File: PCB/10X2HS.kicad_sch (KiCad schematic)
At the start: 23 parts, among them SW1 SW, SW10 SW, SW11 SW, SW12 SW, SW13 SW, SW14 SW, SW15 SW, SW16 SW, SW17 SW, SW18 SW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

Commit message: more updates I guess
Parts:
- removed SW22: SW_Push, Button_Switch_SMD:Panasonic_EVQPUL_EVQPUC, symbol Switch:SW_Push
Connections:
- net SOFT_OFF: no longer names the net of U2.12 (3V3)
- no-connect marks 0 -> 1
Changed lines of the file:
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@@
 		(color 0 0 0 0)
+	)
+	(no_connect
+		(at 64.77 73.66)
 	)
 	(wire
@@
 		)
 	)
-	(global_label "SOFT_OFF"
-		(shape input)
-		(at 88.9 100.33 180)
-		(effects
-			(font
-				(size 1.27 1.27)
-			)
-			(justify right)
-		)
-		(property "Intersheetrefs" "${INTERSHEET_REFS}"
-			(at 88.9 100.33 0)
-			(effects
-				(font
-					(size 1.27 1.27)
-				)
-				(hide yes)
-			)
-		)
-	)
 	(global_label "SW17"
 		(shape input)
@@
 		)
 	)
-	(global_label "GND"
-		(shape input)
-		(at 99.06 100.33 0)
-		(effects
-			(font
-				(size 1.27 1.27)
-			)
-			(justify left)
-		)
-		(property "Intersheetrefs" "${INTERSHEET_REFS}"
-			(at 99.06 100.33 0)
-			(effects
-				(font
-					(size 1.27 1.27)
-				)
-				(hide yes)
-			)
-		)
-	)
 	(global_label "VCC"
 		(shape input)
@@
 		(property "Intersheetrefs" "${INTERSHEET_REFS}"
 			(at 64.77 91.44 0)
-			(effects
-				(font
-					(size 1.27 1.27)
-				)
-				(hide yes)
-			)
-		)
-	)
-	(global_label "SOFT_OFF"
-		(shape input)
-		(at 64.77 73.66 0)
-		(effects
-			(font
-				(size 1.27 1.27)
-			)
-			(justify left)
-		)
-		(property "Intersheetrefs" "${INTERSHEET_REFS}"
-			(at 64.77 73.66 0)
 			(effects
 				(font
@@
 					(unit 1)
 				)
-			)
-		)
-	)
-	(symbol
-		(lib_id "Switch:SW_Push")
-		(at 93.98 100.33 0)
-		(unit 1)
-		(exclude_from_sim no)
-		(in_bom yes)
-		(on_board yes)
-		(dnp no)
-		(fields_autoplaced yes)
-		(property "Reference" "SW22"
-			(at 93.98 92.71 0)
-			(effects
-				(font
-					(size 1.27 1.27)
-				)
-			)
-		)
-		(property "Value" "SW_Push"
-			(at 93.98 95.25 0)
-			(effects
-				(font
-					(size 1.27 1.27)
-				)
-			)
-		)
-		(property "Footprint" "Button_Switch_SMD:Panasonic_EVQPUL_EVQPUC"
-			(at 93.98 95.25 0)
-			(effects
-				(font
-					(size 1.27 1.27)
-				)
-				(hide yes)
-			)
-		)
-		(property "Datasheet" "~"
-			(at 93.98 95.25 0)
-			(effects
-				(font
-					(size 1.27 1.27)
-				)
-				(hide yes)
-			)
-		)
-		(property "Description" "Push button switch, generic, two pins"
-			(at 93.98 100.33 0)
-			(effects
-				(font
-					(size 1.27 1.27)
-				)
-				(hide yes)
-			)
-		)
-		(pin "1"
-		)
-		(pin "2"
-		)
-		(instances
-			(project ""
-				(path "/31ee86e8-2846-4d2f-8bbd-b1d272a4eb8b"
-					(reference "SW22")
-					(unit 1)
-				)

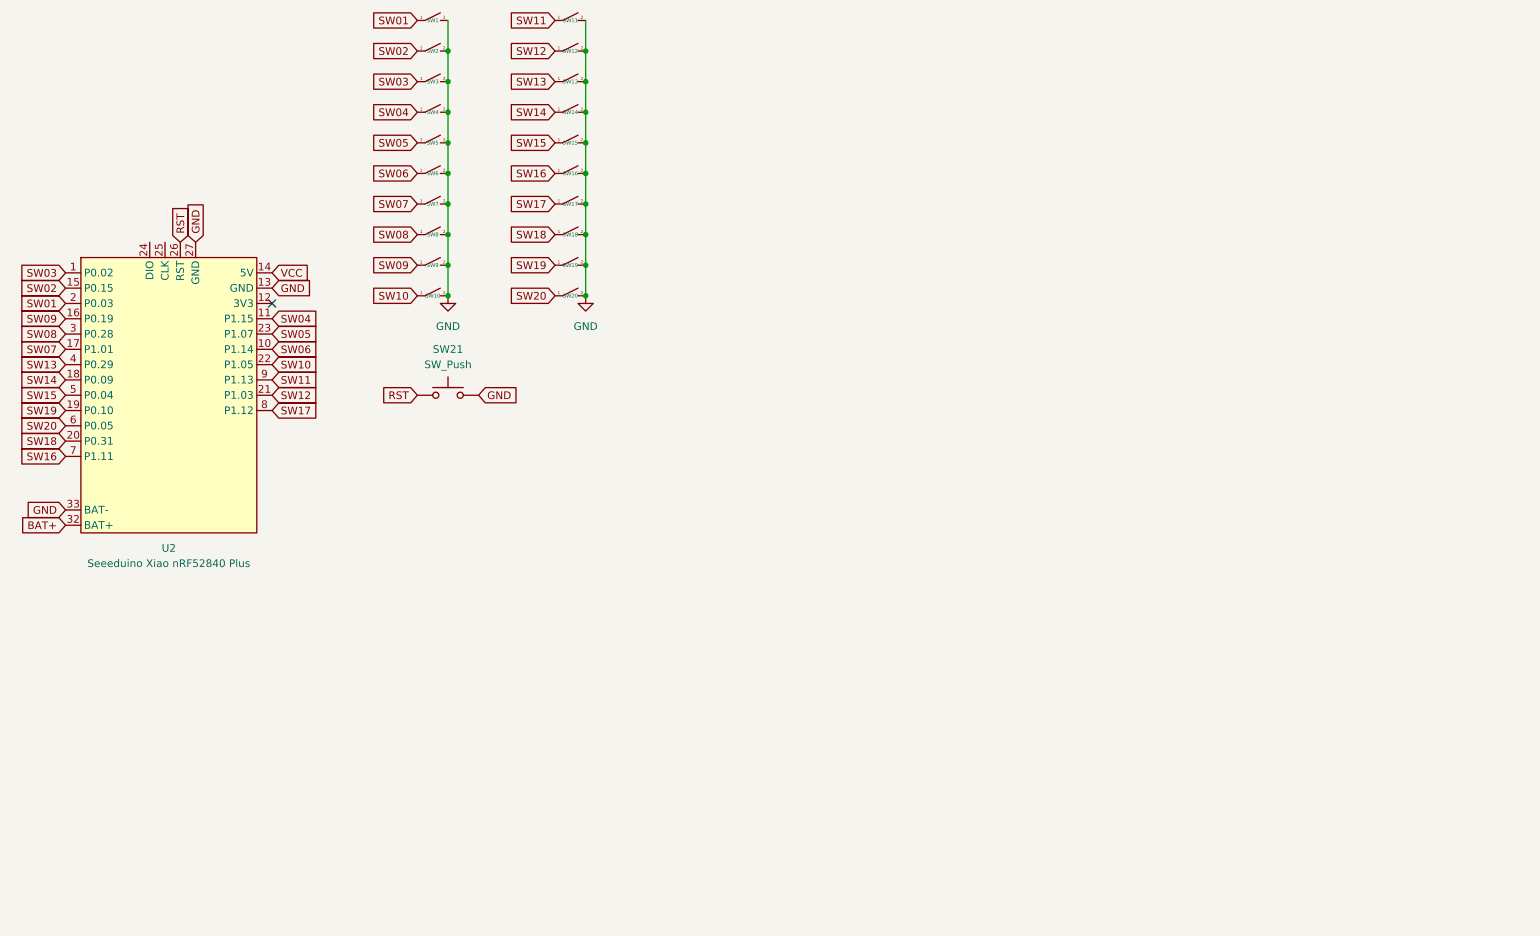
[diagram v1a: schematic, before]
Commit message: changed to nonplus xiao, add direct battery pads
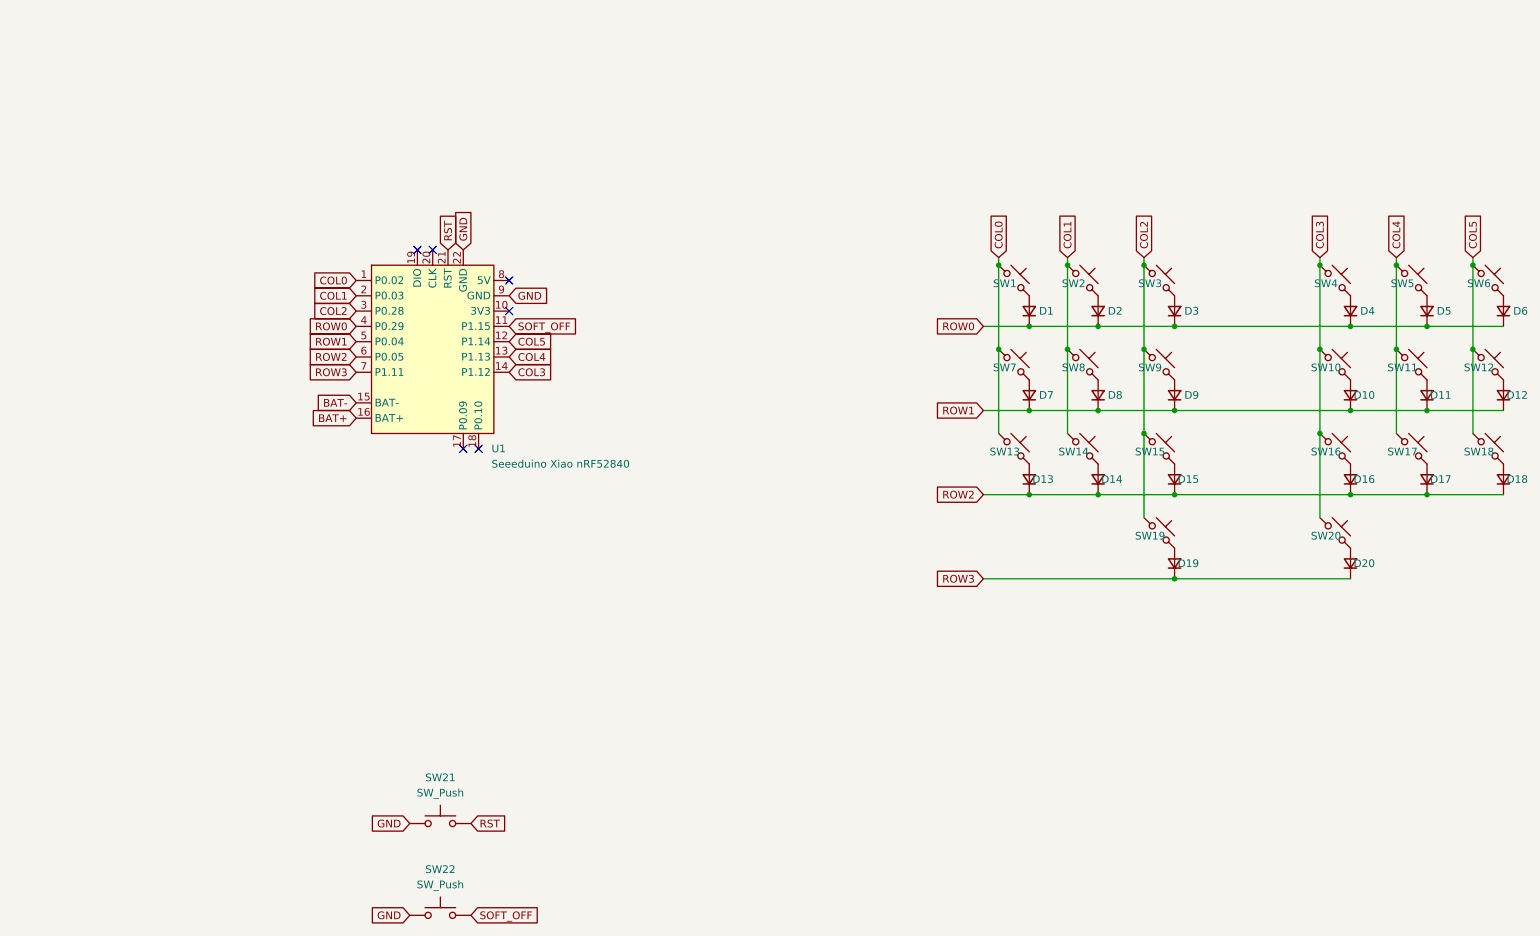
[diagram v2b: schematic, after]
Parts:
- removed SW1, SW10, SW11, SW12, SW13, SW14, SW15, SW16, SW17, SW18, SW19, SW2, SW20, SW3, SW4, SW5, SW6, SW7, SW8, SW9: SW, miketronic_fplib:MB_KailhChoc-1U_rev_17mm_oval, symbol hazel:SW
- removed U2: Seeeduino Xiao nRF52840 Plus, xiao nrf52840 plus:XIAO-nRF52840-Plus-SMD, symbol xiao nrf plus:Seeeduino_Xiao_nRF52840_Plus
- added D1, D10, D11, D12, D13, D14, D15, D16, D17, D18, D19, D2, D20, D3, D4, D5, D6, D7, D8, D9: 1n4148, zackforbing:D_SOD-123, symbol Device:D_Small
- added SW1, SW10, SW11, SW12, SW13, SW14, SW15, SW16, SW17, SW18, SW19, SW2, SW20, SW3, SW4, SW5, SW6, SW7, SW8, SW9: MX_SW_solder, marbastlib-mx:SW_MX_1u_rev, symbol marbastlib-mx:MX_SW_solder
- added SW22: SW_Push, Button_Switch_THT:SW_PUSH_6mm, symbol Switch:SW_Push
- added U1: Seeeduino Xiao nRF52840, PCM_marbastlib-xp-promicroish:Xiao_nRF52840_ACH, symbol PCM_marbastlib-promicroish:Seeeduino_Xiao_nRF52840
- SW21: footprint Button_Switch_SMD:Panasonic_EVQPUL_EVQPUC -> Button_Switch_THT:SW_PUSH_6mm
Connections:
- net BAT+: now also U1.16 (BAT+)
- net GND: now also SW21.1, SW22.1, U1.22 (GND), U1.9 (GND); no longer SW21.2
- net RST: now also SW21.2, U1.21 (RST); no longer SW21.1
- new net: D7.2 (A), SW7.2
- new net: D19.2 (A), SW19.2
- new net: D1.2 (A), SW1.2
- new net: D11.2 (A), SW11.2
- new net: D18.2 (A), SW18.2
- new net: D4.2 (A), SW4.2
- new net: D13.2 (A), SW13.2
- new net: D3.2 (A), SW3.2
- new net: D16.2 (A), SW16.2
- new net: D12.2 (A), SW12.2
- new net: D6.2 (A), SW6.2
- new net: D17.2 (A), SW17.2
- new net: D9.2 (A), SW9.2
- new net: D2.2 (A), SW2.2
- new net: D14.2 (A), SW14.2
- new net: D10.2 (A), SW10.2
- new net: D20.2 (A), SW20.2
- new net: D15.2 (A), SW15.2
- new net: D5.2 (A), SW5.2
- new net: D8.2 (A), SW8.2
- new net BAT-: U1.15 (BAT-)
- new net COL0: SW1.1, SW13.1, SW7.1, U1.1 (P0.02)
- new net COL1: SW14.1, SW2.1, SW8.1, U1.2 (P0.03)
- new net COL2: SW15.1, SW19.1, SW3.1, SW9.1, U1.3 (P0.28)
- new net COL3: SW10.1, SW16.1, SW20.1, SW4.1, U1.14 (P1.12)
- new net COL4: SW11.1, SW17.1, SW5.1, U1.13 (P1.13)
- new net COL5: SW12.1, SW18.1, SW6.1, U1.12 (P1.14)
- new net ROW0: D1.1 (K), D2.1 (K), D3.1 (K), D4.1 (K), D5.1 (K), D6.1 (K), U1.4 (P0.29)
- new net ROW1: D10.1 (K), D11.1 (K), D12.1 (K), D7.1 (K), D8.1 (K), D9.1 (K), U1.5 (P0.04)
- new net ROW2: D13.1 (K), D14.1 (K), D15.1 (K), D16.1 (K), D17.1 (K), D18.1 (K), U1.6 (P0.05)
- new net ROW3: D19.1 (K), D20.1 (K), U1.7 (P1.11)
- new net SOFT_OFF: SW22.2, U1.11 (P1.15)
- no-connect marks 1 -> 6
